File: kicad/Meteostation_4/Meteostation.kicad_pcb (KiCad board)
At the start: 2 copper layers, 44 x 44 mm, 106 parts, among them J1 TxD, J10 GM+, J11 GM-, J12 SWD, J13 SWC, J2 RxD, J3 BME280_SCL, J4 BME280_SDA, J6 +EXT, J7 -EXT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

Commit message: изменено:      kicad/Meteostation_4/Meteostation.kicad_pcb 	изменено:      kicad/Meteostation_4/Meteostation.kicad_pcb-bak 	изменено:      kicad/Meteostation_4/Meteostation.sch 	изменено:      kicad/Meteostation_4/Meteostation.sch-bak 	изменено:      kicad/Meteostation_4/fp-info-cache 	изменено:      kicad/Meteostation_4/gerber/Meteostation-job.gbrjob
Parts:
- added J14: DISP_CS, My-library:ConnMini, F.Cu at (53.0, 89.2)
- added J5: miso, My-library:ConnMini, F.Cu at (54.2, 88.8)
- added J8: mosi, My-library:ConnMini, F.Cu at (53.4, 90.7)
- added J9: sclk, My-library:ConnMini, F.Cu at (55.2, 89.5)
- R4: footprint Resistor_SMD:R_0603_1608Metric -> Resistor_SMD:R_0402_1005Metric
- moved D4 0.85 mm to (51.7, 88.4)
- moved R4 0.64 mm to (51.7, 90.8)
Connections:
- U1 pad 30: (no net) -> Net-(J14-Pad1)
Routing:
- net Net-(J14-Pad1): track 0.00 -> 3.90 mm
- net MISO: track 6.47 -> 7.56 mm

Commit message: изменено:      kicad/Meteostation_4/Meteostation.kicad_pcb 	изменено:      kicad/Meteostation_4/Meteostation.kicad_pcb-bak
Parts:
- moved D9 3.46 mm to (22.9, 90.2), turned to 180 degrees
- moved Q1 3.03 mm to (22.8, 94.5), turned to 270 degrees
- moved D6 2.84 mm to (23.2, 85.4)
- moved R23 2.30 mm to (22.4, 87.9)
- moved R24 0.54 mm to (22.4, 91.9), turned to 180 degrees
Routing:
- net Net-(D9-Pad2): track 77.4 -> 73.1 mm
- net Net-(C19-Pad2): track 43.2 -> 46.2 mm
- net Net-(D9-Pad1): track 4.43 -> 7.13 mm
- net Net-(C19-Pad1): track 92.9 -> 92.1 mm

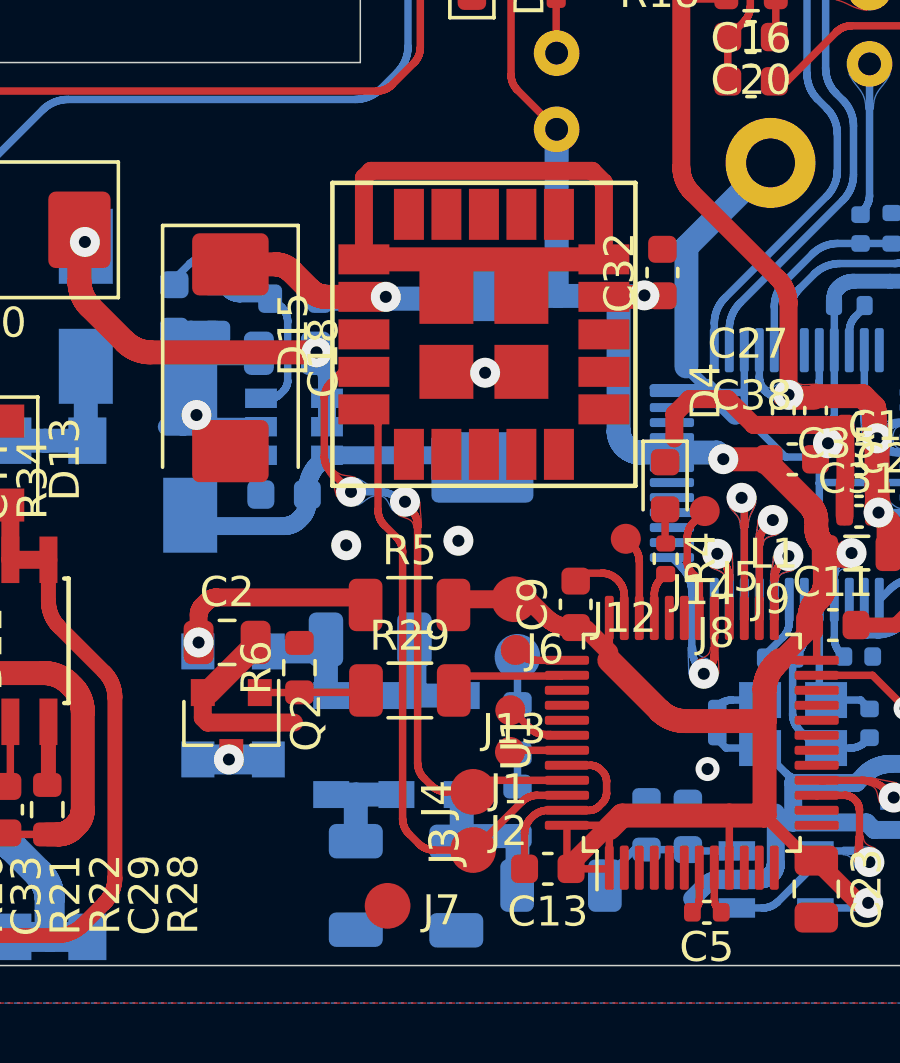
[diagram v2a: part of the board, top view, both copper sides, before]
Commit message: изменено:      Documents/sheet.png 	изменено:      kicad/Meteostation_4/Meteostation-cache.lib 	изменено:      kicad/Meteostation_4/Meteostation.kicad_pcb 	изменено:      kicad/Meteostation_4/Meteostation.kicad_pcb-bak 	изменено:      kicad/Meteostation_4/Meteostation.sch 	изменено:      kicad/Meteostation_4/Meteostation.sch-bak 	изменено:      kicad/Meteostation_4/fp-info-cache 	изменено:      stm32cubeide/Meteostation/.mxproject 	изменено:      stm32cubeide/Meteostation/.settings/language.settings.xml 	изменено:      stm32cubeide/Meteostation/Core/Inc/main.h 	изменено:      stm32cubeide/Meteostation/Core/Src/main.c 	изменено:      stm32cubeide/Meteostation/Meteostation.ioc 	изменено:      stm32cubeide/Meteostation/Release/Core/Src/main.o 	изменено:      stm32cubeide/Meteostation/Release/Core/Src/main.su 	изменено:      stm32cubeide/Meteostation/Release/Meteostation.bin 	изменено:      stm32cubeide/Meteostation/Release/Meteostation.elf 	изменено:      stm32cubeide/Meteostation/Release/Meteostation.hex 	изменено:      stm32cubeide/Meteostation/Release/Meteostation.list 	изменено:      stm32cubeide/Meteostation/Release/Meteostation.map 	изменено:      stm32cubeide/Meteostation/Release/makefile
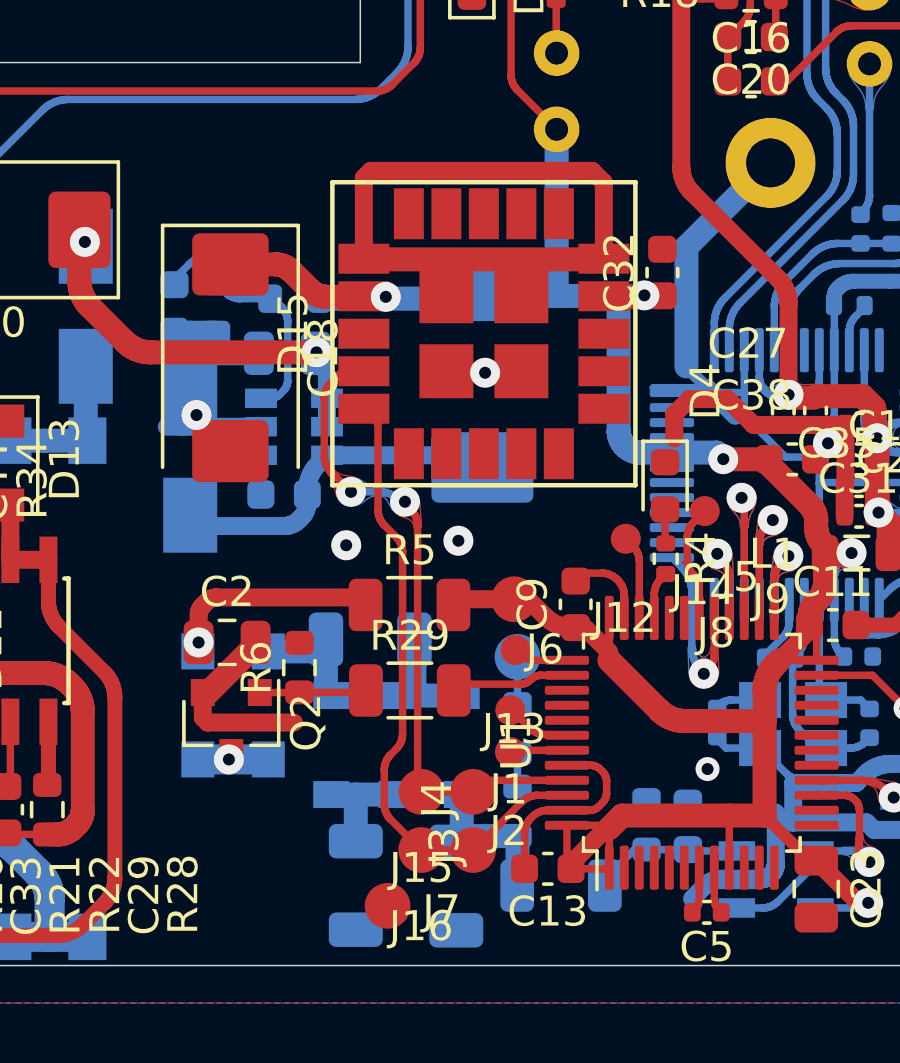
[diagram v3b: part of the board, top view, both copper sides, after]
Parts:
- added J15: OLED_SCL, My-library:SMD-CONN, F.Cu at (43.5, 98.6)
- added J16: OLED_SDA, My-library:SMD-CONN, F.Cu at (43.5, 100.5)
- D10: value SS56 -> SS56, VS10MQ060-M3/5
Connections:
- D15 pad 1: (no net) -> GND
- D15 pad 11: (no net) -> GND
- D15 pad 12: (no net) -> GND
- D15 pad 13: (no net) -> GND
- D15 pad 14: (no net) -> GND
- D15 pad 15: (no net) -> GND
- D15 pad 16: (no net) -> GND
- D15 pad 17: (no net) -> GND
- D15 pad 18: (no net) -> GND
- D15 pad 2: (no net) -> GND
- D15 pad 3: (no net) -> GND
- D15 pad 4: (no net) -> GND
- D15 pad 5: (no net) -> GND
- D15 pad 8: (no net) -> GND
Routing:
- net SDA: track 20.9 -> 21.5 mm

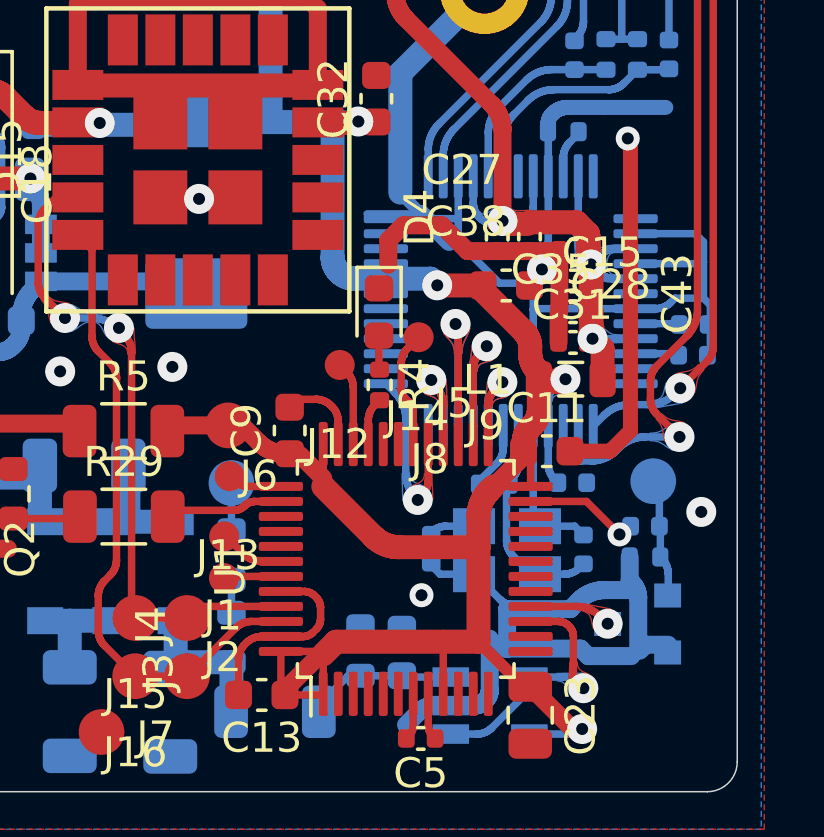
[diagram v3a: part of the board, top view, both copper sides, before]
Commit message: изменено:      Arduino/meteomonitor/meteomonitor.ino 	изменено:      FreeCAD/GM_case_top.FCStd 	изменено:      kicad/Meteostation_4/Meteostation-cache.lib 	изменено:      kicad/Meteostation_4/Meteostation-rescue.lib 	изменено:      kicad/Meteostation_4/Meteostation.kicad_pcb 	изменено:      kicad/Meteostation_4/Meteostation.kicad_pcb-bak 	изменено:      kicad/Meteostation_4/Meteostation.sch 	изменено:      kicad/Meteostation_4/Meteostation.sch-bak 	изменено:      kicad/Meteostation_4/fp-info-cache 	изменено:      stm32cubeide/Meteostation/.cproject 	изменено:      stm32cubeide/Meteostation/.mxproject 	изменено:      stm32cubeide/Meteostation/.settings/language.settings.xml 	изменено:      stm32cubeide/Meteostation/Core/Inc/main.h 	изменено:      stm32cubeide/Meteostation/Core/Inc/stm32f1xx_it.h 	изменено:      stm32cubeide/Meteostation/Core/Src/BME280.c 	изменено:      stm32cubeide/Meteostation/Core/Src/main.c 	изменено:      stm32cubeide/Meteostation/Core/Src/stm32f1xx_hal_msp.c 	изменено:      stm32cubeide/Meteostation/Core/Src/stm32f1xx_it.c 	изменено:      stm32cubeide/Meteostation/Meteostation.ioc 	изменено:      stm32cubeide/Meteostation/Meteostation.launch 	изменено:      stm32cubeide/Meteostation/Release/Core/Src/BME280.d 	изменено:      stm32cubeide/Meteostation/Release/Core/Src/BME280.o 	изменено:      stm32cubeide/Meteostation/Release/Core/Src/main.d 	изменено:      stm32cubeide/Meteostation/Release/Core/Src/main.o 	изменено:      stm32cubeide/Meteostation/Release/Core/Src/main.su 	изменено:      stm32cubeide/Meteostation/Release/Core/Src/stm32f1xx_hal_msp.d 	изменено:      stm32cubeide/Meteostation/Release/Core/Src/stm32f1xx_hal_msp.o 	изменено:      stm32cubeide/Meteostation/Release/Core/Src/stm32f1xx_hal_msp.su 	изменено:      stm32cubeide/Meteostation/Release/Core/Src/stm32f1xx_it.d 	изменено:      stm32cubeide/Meteostation/Release/Core/Src/stm32f1xx_it.o 	изменено:      stm32cubeide/Meteostation/Release/Core/Src/stm32f1xx_it.su 	изменено:      stm32c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
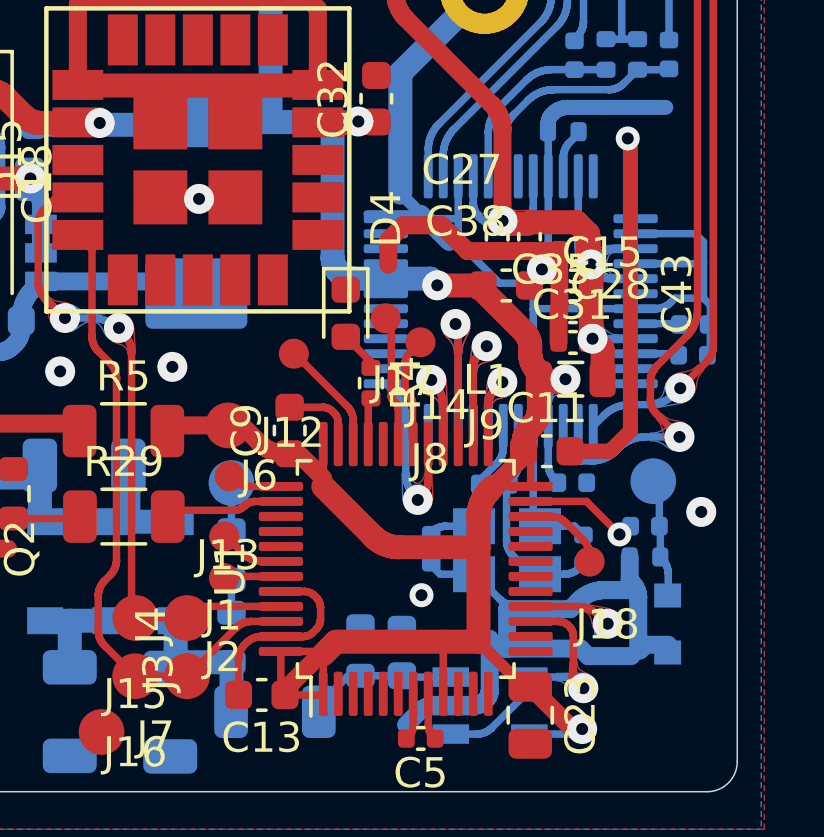
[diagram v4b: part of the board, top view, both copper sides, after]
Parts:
- removed J5: miso, My-library:ConnMini
- added J17: ST7735S_DC, My-library:mini_conn, F.Cu at (51.9, 88.6)
- added J18: ST7735S_RESET, My-library:mini_conn, F.Cu at (58.7, 96.7)
- J14: value DISP_CS -> ST7735S_CS; footprint My-library:ConnMini -> My-library:mini_conn
- R4: value 1k -> 4.7k
- moved J12 1.58 mm to (48.8, 89.8)
- moved D4 1.11 mm to (50.5, 88.5)
- moved R4 0.30 mm to (51.4, 90.8)
- moved J14 0.18 mm to (53.0, 89.4)
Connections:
- U1 pad 22: (no net) -> Net-(J18-Pad1)
- U1 pad 31: (no net) -> Net-(J17-Pad1)
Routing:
- net Net-(J17-Pad1): track 0.00 -> 4.35 mm
- net Net-(J18-Pad1): track 0.00 -> 2.83 mm
- net Net-(J12-Pad1): track 2.79 -> 3.82 mm

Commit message: изменено:      kicad/Meteostation_4/Meteostation.kicad_pcb 	изменено:      kicad/Meteostation_4/Meteostation.kicad_pcb-bak 	изменено:      kicad/Meteostation_4/Meteostation.sch 	изменено:      kicad/Meteostation_4/Meteostation.sch-bak 	изменено:      kicad/Meteostation_4/gerber/Border.gbr 	изменено:      kicad/Meteostation_4/gerber/Bottom.gbr 	изменено:      kicad/Meteostation_4/gerber/MaskBottom.gbr 	изменено:      kicad/Meteostation_4/gerber/MaskTop.gbr 	изменено:      kicad/Meteostation_4/gerber/Meteostation-job.gbrjob 	изменено:      kicad/Meteostation_4/gerber/Meteostation.zip 	изменено:      kicad/Meteostation_4/gerber/NCData.drl 	изменено:      kicad/Meteostation_4/gerber/Top.gbr
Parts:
- removed D10: SS56, VS10MQ060-M3/5, Diode_SMD:D_SMA
- added J5: +EXT, My-library:ConnMini, F.Cu at (46.6, 90.5)
- C19: value 22uF/63v -> 100uF/63v; footprint Capacitor_SMD:CP_Elec_6.3x7.7 -> My-library:CAP_horizontal
- C22: footprint Capacitor_SMD:C_0603_1608Metric -> Capacitor_SMD:C_0402_1005Metric
- R13: value 5G -> HVC1206Z5007KET
- R16: footprint Resistor_SMD:R_0603_1608Metric -> Resistor_SMD:R_0402_1005Metric
- U2: value LMR14206 -> LMR50410XDBVR
- moved C30 4.37 mm to (39.3, 80.7), turned to 180 degrees
- moved C19 4.33 mm to (28.4, 78.8), turned to 270 degrees
- moved D16 2.84 mm to (30.1, 84.2), turned to 0 degrees
- moved D4 1.35 mm to (51.6, 87.5)
- moved J12 1.26 mm to (49.9, 90.4)
- moved J17 1.20 mm to (52.9, 88.0)
- moved C18 1.03 mm to (37.2, 85.2)
- moved R13 0.95 mm to (48.9, 101.1)
- moved R20 0.91 mm to (47.1, 95.7)
- moved J13 0.83 mm to (45.9, 93.7)
- moved J10 0.82 mm to (46.4, 93.3)
- moved R17 0.80 mm to (47.1, 98.6)
- moved R16 0.64 mm to (51.6, 100.1)
- moved C3 0.64 mm to (42.5, 93.5)
- moved R8 0.44 mm to (36.7, 82.9)
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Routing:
- net GND: track 166.7 -> 196.3 mm, vias 10 -> 11
- net Net-(C19-Pad1): track 92.1 -> 97.7 mm
- net 12-16: track 13.3 -> 18.7 mm
- net Net-(C8-Pad2): track 11.7 -> 6.88 mm
- net +3.3VDAC: track 110.1 -> 107.1 mm
- net Net-(J12-Pad1): track 3.82 -> 2.72 mm
- net Net-(C22-Pad2): track 4.82 -> 3.93 mm
- net Net-(J13-Pad1): track 1.82 -> 2.71 mm
- net Net-(J17-Pad1): track 4.35 -> 5.17 mm
- net Net-(D4-Pad2): track 1.38 -> 2.01 mm
- net Net-(C3-Pad2): track 4.03 -> 4.60 mm
- net Net-(D14-Pad6): track 7.30 -> 7.80 mm

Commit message: изменено:      FreeCAD/GM_case.FCStd 	изменено:      kicad/BME280/BME280.kicad_pcb 	изменено:      kicad/Meteostation_4/Meteostation-rescue.lib 	изменено:      kicad/Meteostation_4/Meteostation.kicad_pcb 	изменено:      stm32cubeide/Meteostation/.settings/language.settings.xml 	изменено:      stm32cubeide/Meteostation/Core/Inc/main.h 	изменено:      stm32cubeide/Meteostation/Core/Src/main.c 	изменено:      stm32cubeide/Meteostation/Meteostation.ioc 	изменено:      stm32cubeide/Meteostation/Meteostation.launch 	изменено:      stm32cubeide/Meteostation/Release/Core/Src/main.o 	изменено:      stm32cubeide/Meteostation/Release/Core/Src/main.su 	изменено:      stm32cubeide/Meteostation/Release/Core/Src/stm32f1xx_it.o 	изменено:      stm32cubeide/Meteostation/Release/Meteostation.bin 	изменено:      stm32cubeide/Meteostation/Release/Meteostation.elf 	изменено:      stm32cubeide/Meteostation/Release/Meteostation.hex 	изменено:      stm32cubeide/Meteostation/Release/Meteostation.list 	изменено:      stm32cubeide/Meteostation/Release/Meteostation.map
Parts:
- R7: value 3.4k -> 51k
- R8: value 1.02k -> 22.1k
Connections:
- D3 pad 12: (no net) -> unconnected-(D3-Pad12)
- D3 pad 13: (no net) -> unconnected-(D3-Pad13)
- D3 pad 18: (no net) -> unconnected-(D3-Pad18)
- D3 pad 23: (no net) -> unconnected-(D3-Pad23)
- D3 pad 24: (no net) -> unconnected-(D3-Pad24)
- D3 pad 26: (no net) -> unconnected-(D3-Pad26)
- D3 pad 36: (no net) -> unconnected-(D3-Pad36)
- D3 pad 38: (no net) -> unconnected-(D3-Pad38)
- D3 pad 39: (no net) -> unconnected-(D3-Pad39)
- D3 pad 40: (no net) -> unconnected-(D3-Pad40)
- D3 pad 41: (no net) -> unconnected-(D3-Pad41)
- D3 pad 42: (no net) -> unconnected-(D3-Pad42)
- D3 pad 46: (no net) -> unconnected-(D3-Pad46)
- D3 pad 47: (no net) -> unconnected-(D3-Pad47)
- D3 pad 7: (no net) -> unconnected-(D3-Pad7)
- U1 pad 10: (no net) -> unconnected-(U1-Pad10)
- U1 pad 11: (no net) -> unconnected-(U1-Pad11)
- U1 pad 12: (no net) -> unconnected-(U1-Pad12)
- U1 pad 13: (no net) -> unconnected-(U1-Pad13)
- U1 pad 14: (no net) -> unconnected-(U1-Pad14)
- U1 pad 17: (no net) -> unconnected-(U1-Pad17)
- U1 pad 18: (no net) -> unconnected-(U1-Pad18)
- U1 pad 19: (no net) -> unconnected-(U1-Pad19)
- U1 pad 2: (no net) -> unconnected-(U1-Pad2)
- U1 pad 20: (no net) -> unconnected-(U1-Pad20)
- U1 pad 21: (no net) -> unconnected-(U1-Pad21)
- U1 pad 3: (no net) -> unconnected-(U1-Pad3)
- U1 pad 32: (no net) -> unconnected-(U1-Pad32)
- U1 pad 39: (no net) -> unconnected-(U1-Pad39)
- U1 pad 4: (no net) -> unconnected-(U1-Pad4)
- U1 pad 40: (no net) -> unconnected-(U1-Pad40)
- U1 pad 41: (no net) -> unconnected-(U1-Pad41)
- U1 pad 5: (no net) -> unconnected-(U1-Pad5)
- U1 pad 6: (no net) -> unconnected-(U1-Pad6)
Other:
- net class Default removed

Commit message: изменено:      kicad/Meteostation_4/Meteostation.kicad_pcb
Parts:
- removed C11, C13, C9: 0.1uF, Capacitor_SMD:C_0603_1608Metric
- removed C23: 0.1uF, Capacitor_SMD:C_0805_2012Metric
- R7: value 51k -> 3.4k
- R8: value 22.1k -> 1.02k
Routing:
- net GND: track 196.3 -> 194.9 mm
